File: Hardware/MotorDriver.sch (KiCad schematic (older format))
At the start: 17 parts, among them J3 Motor2_con, J4 Motor1_con, U12 MCP4725, U13 ina219, U14 A3968, U15 74HC14

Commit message: Add files via upload
HW layout and libs
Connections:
- wire segments 69 -> 70
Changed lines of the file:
@@
 LIBS:L298N
 LIBS:WS2812B
+LIBS:a4973
 LIBS:a3968
 LIBS:lm2675
@@
 $EndComp
 $Comp
-L +24V #PWR054
+L +24V #PWR057
 U 1 1 5A705C4E
 P 4650 1900
-F 0 "#PWR054" H 4650 1750 50  0001 C CNN
+F 0 "#PWR057" H 4650 1750 50  0001 C CNN
 F 1 "+24V" H 4650 2040 50  0000 C CNN
 F 2 "" H 4650 1900 50  0001 C CNN
@@
 $EndComp
 Wire Wire Line
-	4900 2800 4850 2800
-Wire Wire Line
-	4850 2800 4850 2600
+	4850 2800 4900 2800
+Wire Wire Line
+	4850 2550 4850 2800
 Wire Wire Line
 	4650 2900 4900 2900
@@
 $EndComp
 $Comp
-L GND #PWR055
+L GND #PWR058
 U 1 1 5A705C74
 P 6150 2450
-F 0 "#PWR055" H 6150 2200 50  0001 C CNN
+F 0 "#PWR058" H 6150 2200 50  0001 C CNN
 F 1 "GND" H 6150 2300 50  0000 C CNN
 F 2 "" H 6150 2450 50  0001 C CNN
@@
 $EndComp
 $Comp
-L GND #PWR056
+L GND #PWR059
 U 1 1 5A705C7A
 P 6300 3800
-F 0 "#PWR056" H 6300 3550 50  0001 C CNN
+F 0 "#PWR059" H 6300 3550 50  0001 C CNN
 F 1 "GND" H 6300 3650 50  0000 C CNN
 F 2 "" H 6300 3800 50  0001 C CNN
@@
 SCL
 $Comp
-L GND #PWR058
+L GND #PWR060
 U 1 1 5A705C95
 P 3150 4050
-F 0 "#PWR058" H 3150 3800 50  0001 C CNN
+F 0 "#PWR060" H 3150 3800 50  0001 C CNN
 F 1 "GND" H 3150 3900 50  0000 C CNN
 F 2 "" H 3150 4050 50  0001 C CNN
@@
 $EndComp
 $Comp
-L GND #PWR059
+L GND #PWR061
 U 1 1 5A705C9B
 P 2650 3900
-F 0 "#PWR059" H 2650 3650 50  0001 C CNN
+F 0 "#PWR061" H 2650 3650 50  0001 C CNN
 F 1 "GND" H 2650 3750 50  0000 C CNN
 F 2 "" H 2650 3900 50  0001 C CNN
@@
 Motor_Input_2A
 $Comp
-L GND #PWR061
+L GND #PWR062
 U 1 1 5A705CC1
 P 2650 2250
-F 0 "#PWR061" H 2650 2000 50  0001 C CNN
+F 0 "#PWR062" H 2650 2000 50  0001 C CNN
 F 1 "GND" H 2655 2077 50  0000 C CNN
 F 2 "" H 2650 2250 50  0001 C CNN
@@
 Limit_LOWER_M2
 $Comp
-L GND #PWR062
+L GND #PWR063
 U 1 1 5A705CD4
 P 9100 3900
-F 0 "#PWR062" H 9100 3650 50  0001 C CNN
+F 0 "#PWR063" H 9100 3650 50  0001 C CNN
 F 1 "GND" H 9100 3750 50  0000 C CNN
 F 2 "" H 9100 3900 50  0001 C CNN
@@
 $EndComp
 $Comp
-L GND #PWR063
+L GND #PWR064
 U 1 1 5A705CDA
 P 8400 5350
-F 0 "#PWR063" H 8400 5100 50  0001 C CNN
+F 0 "#PWR064" H 8400 5100 50  0001 C CNN
 F 1 "GND" H 8400 5200 50  0000 C CNN
 F 2 "" H 8400 5350 50  0001 C CNN
@@
 	4650 3900 4350 3900
 $Comp
-L GND #PWR066
+L GND #PWR065
 U 1 1 5A705D02
 P 4350 4250
-F 0 "#PWR066" H 4350 4000 50  0001 C CNN
+F 0 "#PWR065" H 4350 4000 50  0001 C CNN
 F 1 "GND" H 4350 4100 50  0000 C CNN
 F 2 "" H 4350 4250 50  0001 C CNN
@@
 $EndComp
 $Comp
-L GND #PWR067
+L GND #PWR066
 U 1 1 5A705D08
 P 4650 4250
-F 0 "#PWR067" H 4650 4000 50  0001 C CNN
+F 0 "#PWR066" H 4650 4000 50  0001 C CNN
 F 1 "GND" H 4650 4100 50  0000 C CNN
 F 2 "" H 4650 4250 50  0001 C CNN
@@
 	4350 4200 4350 4250
 $Comp
-L GND #PWR068
+L GND #PWR067
 U 1 1 5A705D16
 P 5350 2450
-F 0 "#PWR068" H 5350 2200 50  0001 C CNN
+F 0 "#PWR067" H 5350 2200 50  0001 C CNN
 F 1 "GND" H 5350 2300 50  0000 C CNN
 F 2 "" H 5350 2450 50  0001 C CNN
@@
 Motor Driver
 $Comp
-L GND #PWR070
+L GND #PWR068
 U 1 1 5A705D55
 P 10450 4450
-F 0 "#PWR070" H 10450 4200 50  0001 C CNN
+F 0 "#PWR068" H 10450 4200 50  0001 C CNN
 F 1 "GND" H 10455 4277 50  0000 C CNN
 F 2 "" H 10450 4450 50  0001 C CNN
@@
 	4000 1550 4000 1800
 $Comp
-L GND #PWR072
+L GND #PWR069
 U 1 1 5A705D80
 P 4000 2600
-F 0 "#PWR072" H 4000 2350 50  0001 C CNN
+F 0 "#PWR069" H 4000 2350 50  0001 C CNN
 F 1 "GND" H 4000 2450 50  0000 C CNN
 F 2 "" H 4000 2600 50  0001 C CNN
@@
 	3550 2250 3500 2250
 $Comp
-L GND #PWR073
+L GND #PWR070
 U 1 1 5A705D8B
 P 3100 2150
-F 0 "#PWR073" H 3100 1900 50  0001 C CNN
+F 0 "#PWR070" H 3100 1900 50  0001 C CNN
 F 1 "GND" H 3100 2000 50  0000 C CNN
 F 2 "" H 3100 2150 50  0001 C CNN
@@
 	3100 2050 3100 2150
 $Comp
-L +5V #PWR074
-U 1 1 5A705D94
-P 4850 2600
-F 0 "#PWR074" H 4850 2450 50  0001 C CNN
-F 1 "+5V" H 4850 2740 50  0000 C CNN
-F 2 "" H 4850 2600 50  0001 C CNN
-F 3 "" H 4850 2600 50  0001 C CNN
-	1    4850 2600
-	1    0    0    -1
-$EndComp
-$Comp
-L GND #PWR075
+L GND #PWR071
 U 1 1 5A705D9A
 P 7100 2500
-F 0 "#PWR075" H 7100 2250 50  0001 C CNN
+F 0 "#PWR071" H 7100 2250 50  0001 C CNN
 F 1 "GND" H 7105 2327 50  0000 C CNN
 F 2 "" H 7100 2500 50  0001 C CNN
@@
 $EndComp
 $Comp
-L +5V #PWR076
-U 1 1 5A705DA7
-P 7100 2200
-F 0 "#PWR076" H 7100 2050 50  0001 C CNN
-F 1 "+5V" H 7100 2340 50  0000 C CNN
-F 2 "" H 7100 2200 50  0001 C CNN
-F 3 "" H 7100 2200 50  0001 C CNN
-	1    7100 2200
-	1    0    0    -1
-$EndComp
-$Comp
-L GND #PWR078
+L GND #PWR072
 U 1 1 5A705DB3
 P 2550 4800
-F 0 "#PWR078" H 2550 4550 50  0001 C CNN
+F 0 "#PWR072" H 2550 4550 50  0001 C CNN
 F 1 "GND" H 2555 4627 50  0000 C CNN
 F 2 "" H 2550 4800 50  0001 C CNN
@@
 $EndComp
 $Comp
-L GND #PWR080
+L GND #PWR073
 U 1 1 5A705DC6
 P 10050 4450
-F 0 "#PWR080" H 10050 4200 50  0001 C CNN
+F 0 "#PWR073" H 10050 4200 50  0001 C CNN
 F 1 "GND" H 10055 4277 50  0000 C CNN
 F 2 "" H 10050 4450 50  0001 C CNN
@@
 $EndComp
 $Comp
-L GND #PWR?
+L GND #PWR074
 U 1 1 5A712B0E
 P 6250 6200
-F 0 "#PWR?" H 6250 5950 50  0001 C CNN
+F 0 "#PWR074" H 6250 5950 50  0001 C CNN
 F 1 "GND" H 6250 6050 50  0000 C CNN
 F 2 "" H 6250 6200 50  0001 C CNN
@@
 $EndComp
 $Comp
-L +3.3V #PWR?
+L +3.3V #PWR075
 U 1 1 5A713438
 P 6250 5850
-F 0 "#PWR?" H 6250 5700 50  0001 C CNN
+F 0 "#PWR075" H 6250 5700 50  0001 C CNN
 F 1 "+3.3V" H 6250 5990 50  0000 C CNN
 F 2 "" H 6250 5850 50  0001 C CNN
@@
 	1    0    0    -1
 $EndComp
-$Comp
-L +5V #PWR?
-U 1 1 5A713476
-P 5250 6200
-F 0 "#PWR?" H 5250 6050 50  0001 C CNN
-F 1 "+5V" H 5250 6340 50  0000 C CNN
-F 2 "" H 5250 6200 50  0001 C CNN
-F 3 "" H 5250 6200 50  0001 C CNN
-	1    5250 6200
-	1    0    0    -1
-$EndComp
 Wire Wire Line
 	6250 6100 6250 6200
@@
 	6250 5850 6250 5900
 $Comp
-L +3.3V #PWR?
+L +3.3V #PWR076
 U 1 1 5A713BFF
 P 3150 3000
-F 0 "#PWR?" H 3150 2850 50  0001 C CNN
+F 0 "#PWR076" H 3150 2850 50  0001 C CNN
 F 1 "+3.3V" H 3150 3140 50  0000 C CNN
 F 2 "" H 3150 3000 50  0001 C CNN
@@
 $EndComp
 $Comp
-L +3.3V #PWR?
+L +3.3V #PWR077
 U 1 1 5A713EA2
 P 4000 1550
-F 0 "#PWR?" H 4000 1400 50  0001 C CNN
+F 0 "#PWR077" H 4000 1400 50  0001 C CNN
 F 1 "+3.3V" H 4000 1690 50  0000 C CNN
 F 2 "" H 4000 1550 50  0001 C CNN
@@
 $EndComp
 $Comp
-L +3.3V #PWR?
+L +3.3V #PWR078
 U 1 1 5A713EEC
 P 9250 3750
-F 0 "#PWR?" H 9250 3600 50  0001 C CNN
+F 0 "#PWR078" H 9250 3600 50  0001 C CNN
 F 1 "+3.3V" H 9250 3890 50  0000 C CNN
 F 2 "" H 9250 3750 50  0001 C CNN
@@
 $EndComp
 $Comp
-L +3.3V #PWR?
+L +3.3V #PWR079
 U 1 1 5A713F4B
 P 8450 5150
-F 0 "#PWR?" H 8450 5000 50  0001 C CNN
+F 0 "#PWR079" H 8450 5000 50  0001 C CNN
 F 1 "+3.3V" H 8450 5290 50  0000 C CNN
 F 2 "" H 8450 5150 50  0001 C CNN
@@
 $EndComp
 $Comp
-L +3.3V #PWR?
+L +3.3V #PWR080
 U 1 1 5A713F95
 P 10050 4150
-F 0 "#PWR?" H 10050 4000 50  0001 C CNN
+F 0 "#PWR080" H 10050 4000 50  0001 C CNN
 F 1 "+3.3V" H 10050 4290 50  0000 C CNN
 F 2 "" H 10050 4150 50  0001 C CNN
@@
 $EndComp
 $Comp
-L +3.3V #PWR?
+L +3.3V #PWR081
 U 1 1 5A713FDF
 P 10450 4150
-F 0 "#PWR?" H 10450 4000 50  0001 C CNN
+F 0 "#PWR081" H 10450 4000 50  0001 C CNN
 F 1 "+3.3V" H 10450 4290 50  0000 C CNN
 F 2 "" H 10450 4150 50  0001 C CNN
@@
 $EndComp
 $Comp
-L +3.3V #PWR?
+L +3.3V #PWR082
 U 1 1 5A714C17
 P 2550 4500
-F 0 "#PWR?" H 2550 4350 50  0001 C CNN
+F 0 "#PWR082" H 2550 4350 50  0001 C CNN
 F 1 "+3.3V" H 2550 4640 50  0000 C CNN
 F 2 "" H 2550 4500 50  0001 C CNN
@@
 $EndComp
 $Comp
-L +3.3V #PWR?
+L +3.3V #PWR083
 U 1 1 5A714C61
 P 2650 1950
-F 0 "#PWR?" H 2650 1800 50  0001 C CNN
+F 0 "#PWR083" H 2650 1800 50  0001 C CNN
 F 1 "+3.3V" H 2650 2090 50  0000 C CNN
 F 2 "" H 2650 1950 50  0001 C CNN
@@
 	1    0    0    -1
 $EndComp
+$Comp
+L VDD #PWR084
+U 1 1 5A7C28BC
+P 7100 2150
+F 0 "#PWR084" H 7100 2000 50  0001 C CNN
+F 1 "+5V" H 7100 2300 50  0000 C CNN
+F 2 "" H 7100 2150 50  0001 C CNN
+F 3 "" H 7100 2150 50  0001 C CNN
+	1    7100 2150
+	1    0    0    -1
+$EndComp
+$Comp
+L VDD #PWR085
+U 1 1 5A7C290D
+P 4850 2550
+F 0 "#PWR085" H 4850 2400 50  0001 C CNN
+F 1 "+5V" H 4850 2700 50  0000 C CNN
+F 2 "" H 4850 2550 50  0001 C CNN
+F 3 "" H 4850 2550 50  0001 C CNN
+	1    4850 2550
+	1    0    0    -1
+$EndComp
+Wire Wire Line
+	7100 2200 7100 2150
 $EndSCHEMATC

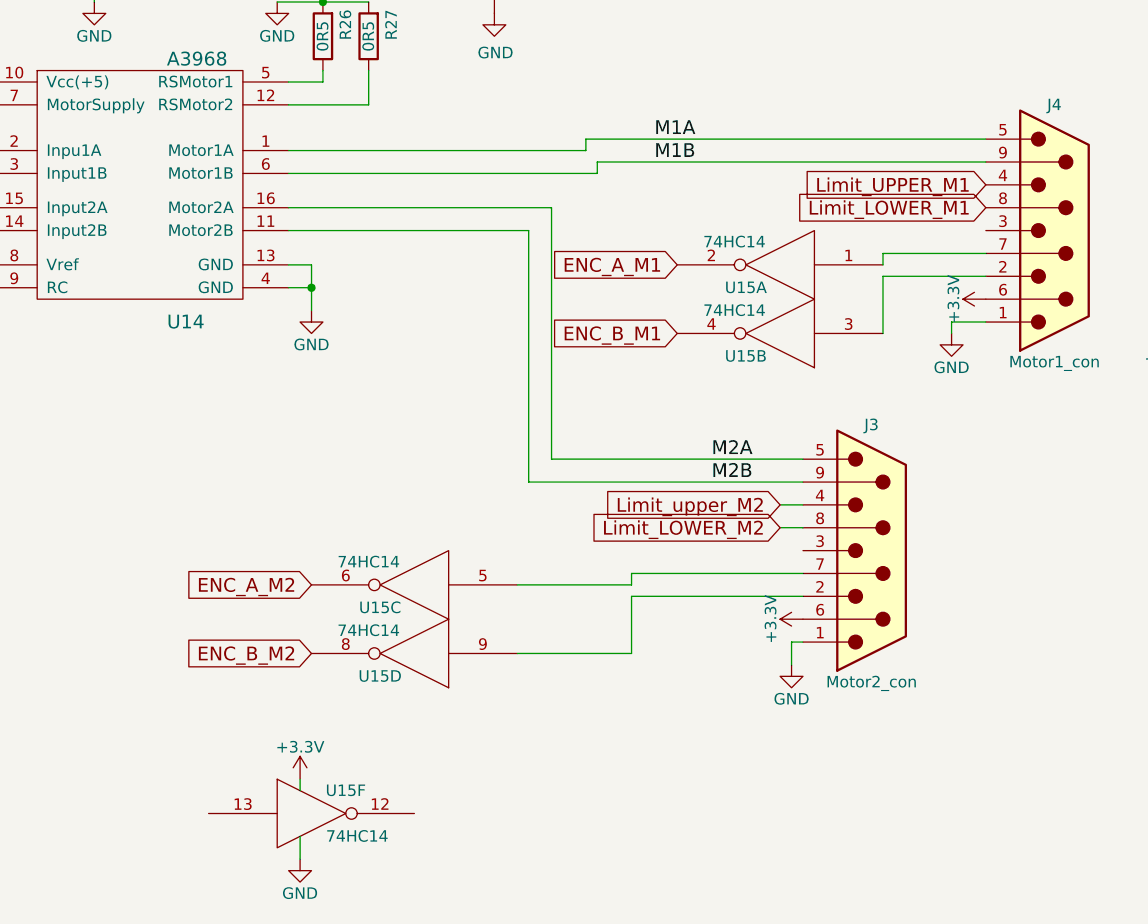
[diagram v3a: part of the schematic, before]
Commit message: one motor
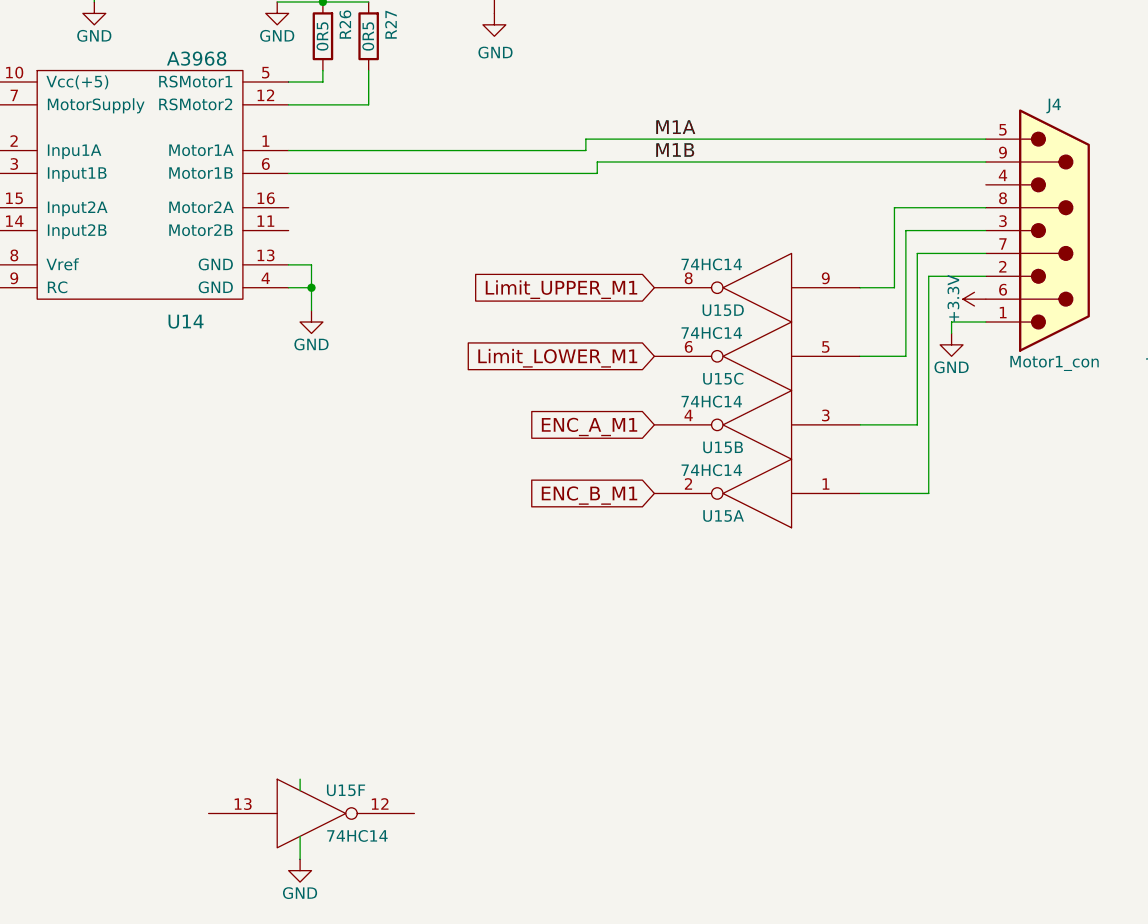
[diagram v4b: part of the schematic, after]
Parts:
- removed J3: Motor2_con, Libs:Dsub9, symbol DB9_Male
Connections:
- net ENC_A_M2 is gone; now on net Limit_LOWER_M1: U15.6
- net ENC_B_M2 is gone; now on net Limit_UPPER_M1: U15.8
- net +3V3: no longer U15.14 (VCC), U15.14 (VCC), U15.14 (VCC), U15.14 (VCC), U15.14 (VCC)
- net ENC_A_M1: now also U15.4; no longer U15.2
- net ENC_B_M1: now also U15.2; no longer U15.4
- net Limit_LOWER_M1: no longer J4.8
- net Limit_UPPER_M1: no longer J4.4
- net at J4.2: now also U15.1; no longer U15.3
- net at J4.3: now also U15.5
- net at J4.7: now also U15.3; no longer U15.1
- net at U15.9: now also J4.8
- net M2A: no longer names the net of U14.16 (Motor2A)
- net M2B: no longer names the net of U14.11 (Motor2B)
- new net VCC: U15.14 (VCC), U15.14 (VCC), U15.14 (VCC), U15.14 (VCC), U15.14 (VCC)
